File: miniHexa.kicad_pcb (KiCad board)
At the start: 2 copper layers, 20 parts, among them U1 STM32F103CBTx, U2 HT7333, Y1 8Mhz

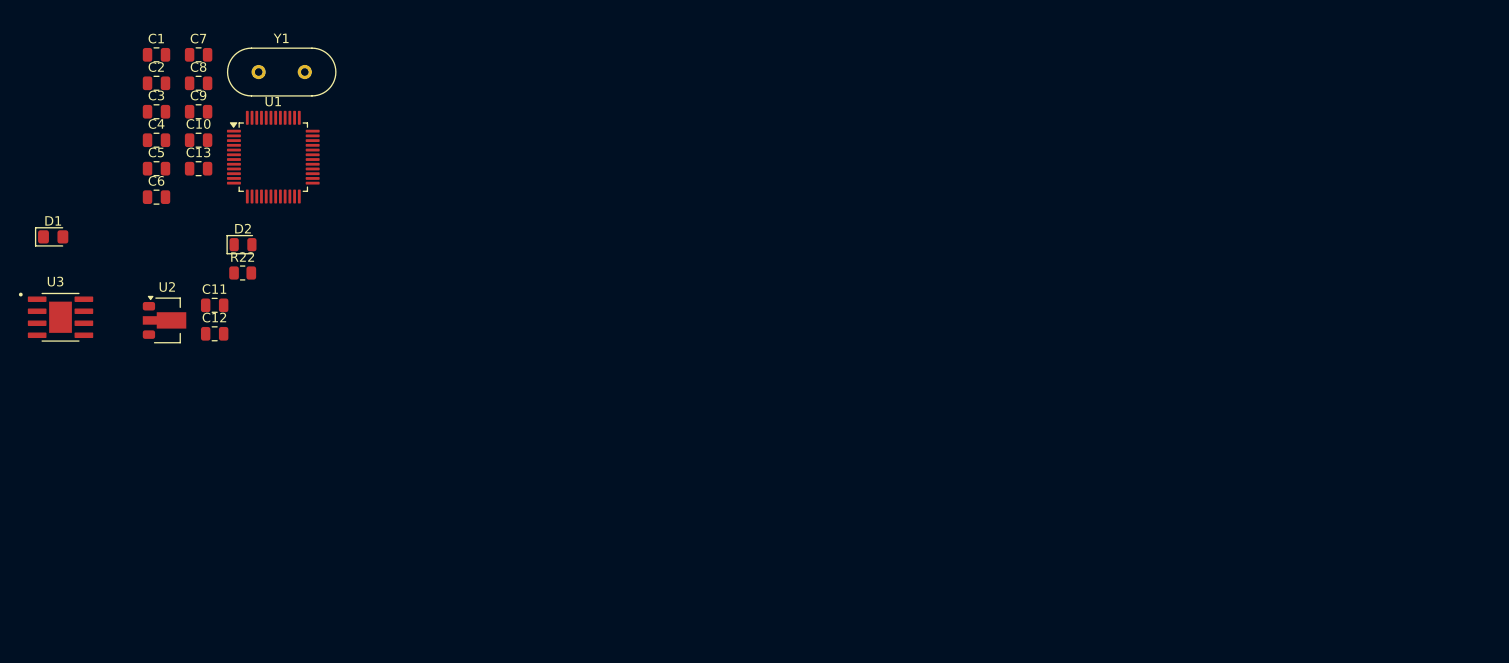
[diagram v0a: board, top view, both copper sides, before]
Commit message: Updated schema
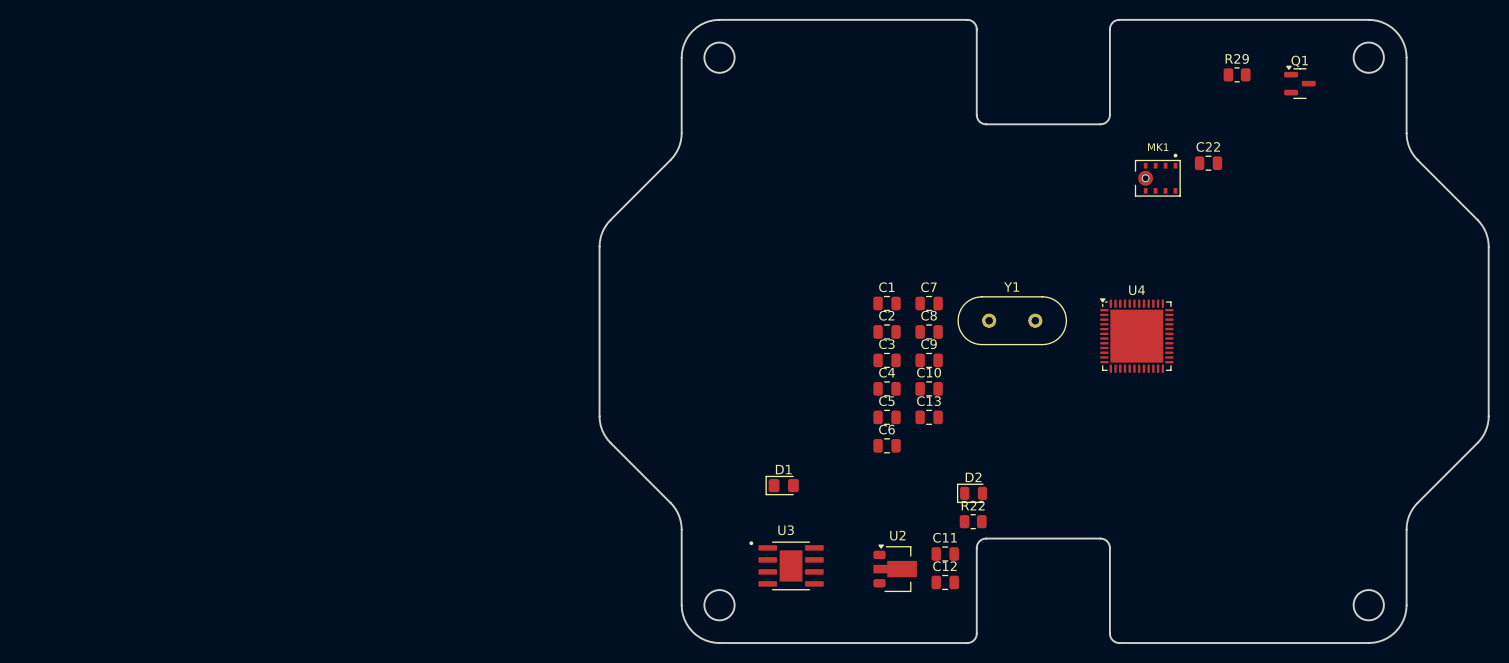
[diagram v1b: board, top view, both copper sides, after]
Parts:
- removed U1: STM32F103CBTx, Package_QFP:LQFP-48_7x7mm_P0.5mm
- added C22: 0.1uF, Capacitor_SMD:C_0805_2012Metric, F.Cu at (181.1, 67.0)
- added MK1: INMP441ACEZ-R7, Microphone:MIC_INMP441ACEZ-R7, F.Cu at (175.8, 68.6)
- added Q1: SS8050, Package_TO_SOT_SMD:SOT-23, F.Cu at (190.8, 58.5)
- added R29: 100, Resistor_SMD:R_0805_2012Metric, F.Cu at (184.2, 57.6)
- added U4: STM32F411CEUx, Package_DFN_QFN:QFN-48-1EP_7x7mm_P0.5mm_EP5.6x5.6mm, F.Cu at (173.6, 85.2)
- moved C11 81.6 mm to (153.3, 108.3)
- moved C12 81.6 mm to (153.3, 111.3)
- moved C2 81.6 mm to (147.1, 84.8)
- moved C8 81.6 mm to (151.6, 84.8)
- moved D2 81.6 mm to (156.3, 101.9)
- moved U2 81.6 mm to (148.3, 109.9)
- moved C1 81.6 mm to (147.1, 81.8)
- moved C10 81.6 mm to (151.6, 90.8)
- moved C13 81.6 mm to (151.6, 93.8)
- moved C3 81.6 mm to (147.1, 87.8)
- moved C4 81.6 mm to (147.1, 90.8)
- moved C5 81.6 mm to (147.1, 93.8)
- moved C6 81.6 mm to (147.1, 96.8)
- moved C7 81.6 mm to (151.6, 81.8)
- moved C9 81.6 mm to (151.6, 87.8)
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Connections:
- net DC_IN renamed Net-(D1-A)
- U3 pad 1: VOUT -> Net-(U3-BOOT)
- U3 pad 4: unconnected-(U3-FB-Pad4) -> FB
- U3 pad 5: unconnected-(U3-EN-Pad5) -> Net-(U3-EN)
- U3 pad 6: unconnected-(U3-GND-Pad6) -> GND
- U3 pad 7: unconnected-(U3-VIN-Pad7) -> VIN
- U3 pad 8: unconnected-(U3-SW-Pad8) -> Net-(D3-K)
- U3 pad 9: (no net) -> GND
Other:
- board outline added: 94 x 65.9 mm

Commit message: update -- i don't remeber what
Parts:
- moved Y1 10.7 mm to (161.6, 73.5)
- turned U4 to -90 degrees

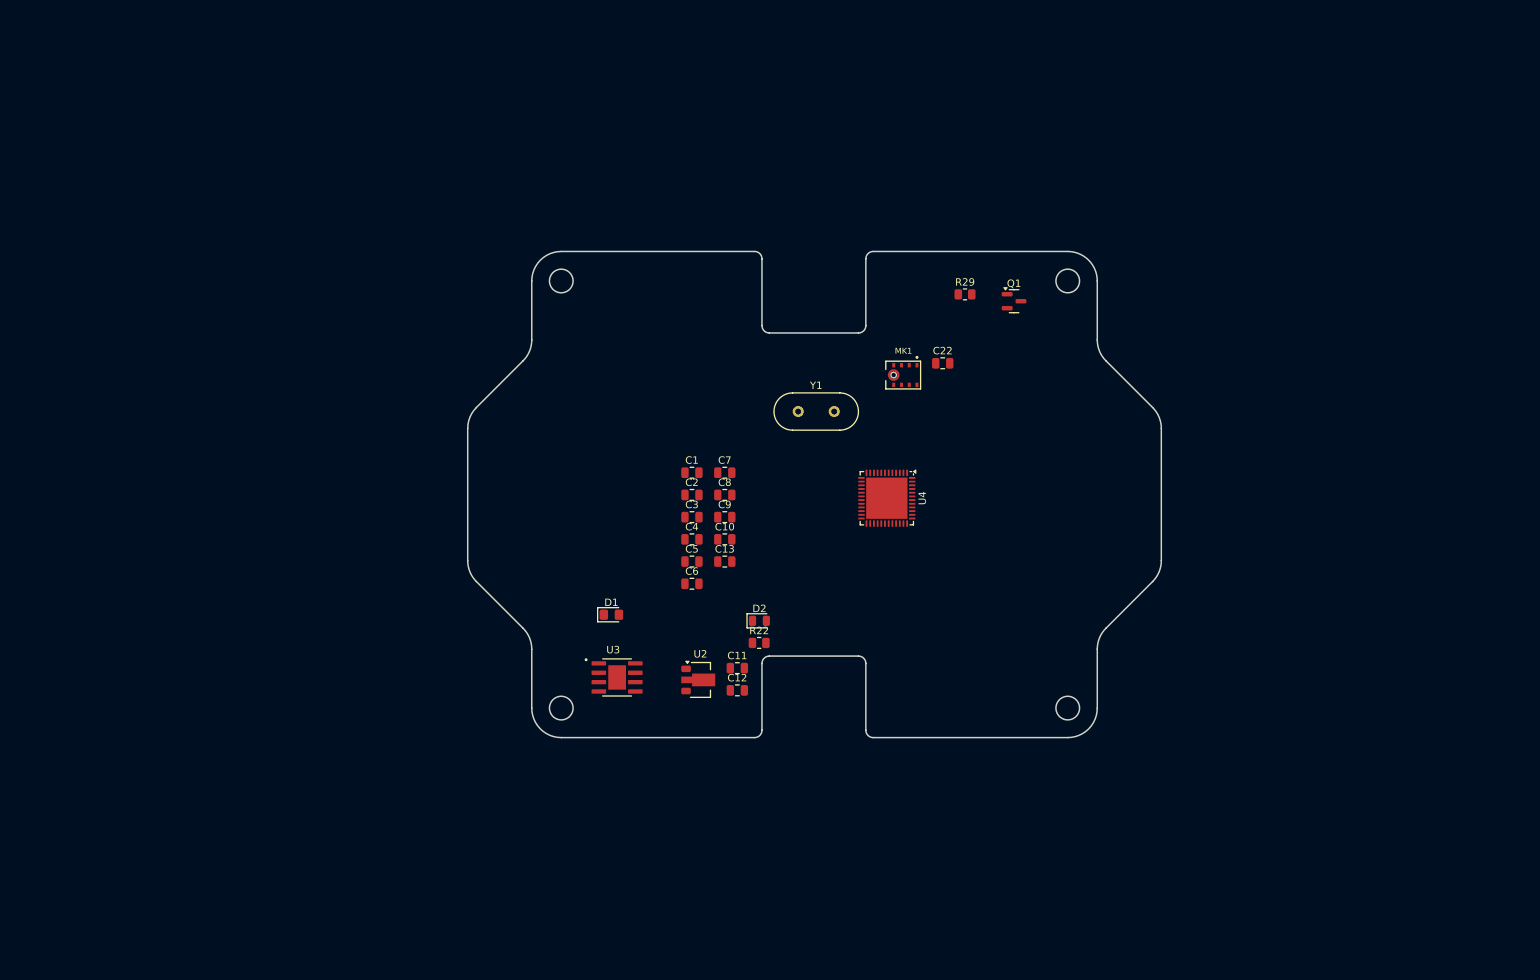
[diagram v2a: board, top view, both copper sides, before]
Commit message: assigned footprints and I2c for stm32
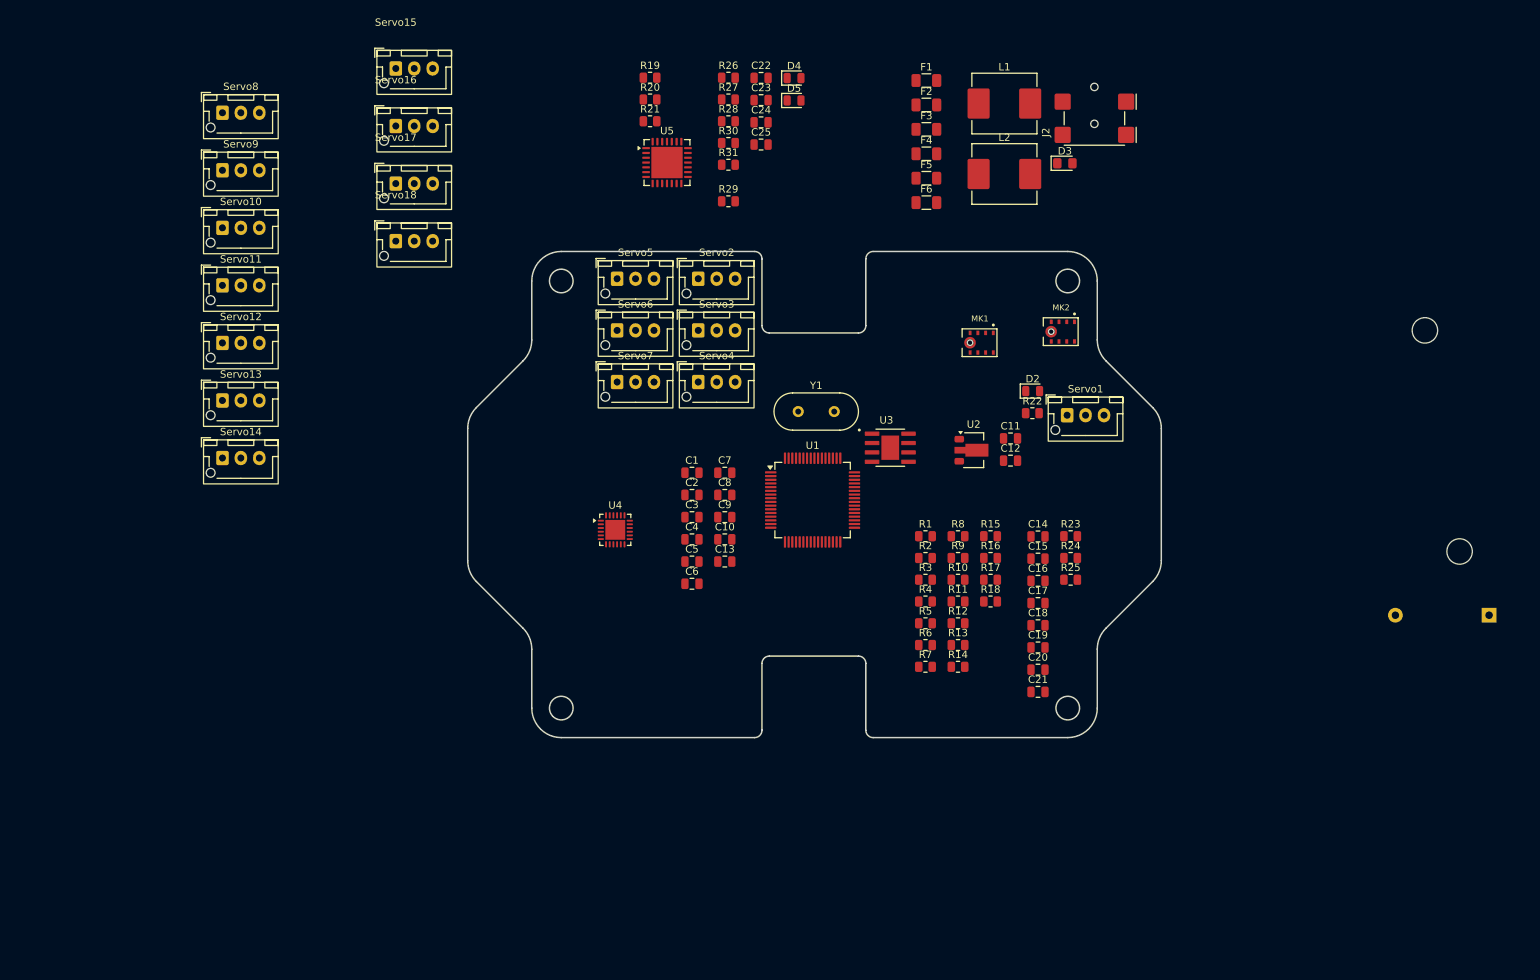
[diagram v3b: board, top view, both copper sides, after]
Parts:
- removed D1: D, Diode_SMD:D_0805_2012Metric_Pad1.15x1.40mm_HandSolder
- removed Q1: SS8050, Package_TO_SOT_SMD:SOT-23
- added BT1: Battery, Battery:BatteryHolder_Keystone_2468_2xAAA, B.Cu at (255.2, 101.1)
- added C14: 10nF, Capacitor_SMD:C_0805_2012Metric, F.Cu at (194.1, 90.4)
- added C15: 4.7uF, Capacitor_SMD:C_0805_2012Metric, F.Cu at (194.1, 93.4)
- added C16: 22uF, Capacitor_SMD:C_0805_2012Metric, F.Cu at (194.1, 96.5)
- added C17: 22uF, Capacitor_SMD:C_0805_2012Metric, F.Cu at (194.1, 99.5)
- added C18: 100uF, Capacitor_SMD:C_0805_2012Metric, F.Cu at (194.1, 102.5)
- added C19: 100uF/10v, Capacitor_SMD:C_0805_2012Metric, F.Cu at (194.1, 105.5)
- added C20: 22uF, Capacitor_SMD:C_0805_2012Metric, F.Cu at (194.1, 108.5)
- added C21: 4.7uF, Capacitor_SMD:C_0805_2012Metric, F.Cu at (194.1, 111.5)
- added C23: C, Capacitor_SMD:C_0805_2012Metric, F.Cu at (156.5, 31.3)
- added C24: C, Capacitor_SMD:C_0805_2012Metric, F.Cu at (156.5, 34.3)
- added C25: C, Capacitor_SMD:C_0805_2012Metric, F.Cu at (156.5, 37.3)
- added D3: P6SMB550A, Diode_SMD:D_0805_2012Metric_Pad1.15x1.40mm_HandSolder, F.Cu at (197.7, 39.8)
- added D4: LED, LED_SMD:LED_0805_2012Metric, F.Cu at (161.0, 28.3)
- added D5: LED, LED_SMD:LED_0805_2012Metric, F.Cu at (161.0, 31.3)
- added F1: 1A, Fuse:Fuse_1206_3216Metric, F.Cu at (178.9, 28.6)
- added F2: 1A, Fuse:Fuse_1206_3216Metric, F.Cu at (178.9, 31.9)
- added F3: 1A, Fuse:Fuse_1206_3216Metric, F.Cu at (178.9, 35.2)
- added F4: 1A, Fuse:Fuse_1206_3216Metric, F.Cu at (178.9, 38.6)
- added F5: 1A, Fuse:Fuse_1206_3216Metric, F.Cu at (178.9, 41.9)
- added F6: 1A, Fuse:Fuse_1206_3216Metric, F.Cu at (178.9, 45.2)
- added J2: 12v DC, Connector_BarrelJack:BarrelJack_Wuerth_694102107102_1.0x3.9mm, F.Cu at (201.7, 32.6)
- added L1: 15uH, Inductor_SMD:L_APV_APH0850, F.Cu at (189.5, 31.8)
- added L2: 15uH, Inductor_SMD:L_APV_APH0850, F.Cu at (189.5, 41.3)
- added MK2: INMP441-R, Audio_Module:MIC_INMP441ACEZ-R7, F.Cu at (197.1, 62.7)
- added R1: 1k, Resistor_SMD:R_0805_2012Metric, F.Cu at (178.8, 90.4)
- added R10: 1k, Resistor_SMD:R_0805_2012Metric, F.Cu at (183.2, 96.3)
- added R11: 1k, Resistor_SMD:R_0805_2012Metric, F.Cu at (183.2, 99.2)
- added R12: 1k, Resistor_SMD:R_0805_2012Metric, F.Cu at (183.2, 102.2)
- added R13: 1k, Resistor_SMD:R_0805_2012Metric, F.Cu at (183.2, 105.2)
- added R14: 1k, Resistor_SMD:R_0805_2012Metric, F.Cu at (183.2, 108.1)
- added R15: 1k, Resistor_SMD:R_0805_2012Metric, F.Cu at (187.6, 90.4)
- added R16: 1k, Resistor_SMD:R_0805_2012Metric, F.Cu at (187.6, 93.3)
- added R17: 1k, Resistor_SMD:R_0805_2012Metric, F.Cu at (187.6, 96.3)
- added R18: 1k, Resistor_SMD:R_0805_2012Metric, F.Cu at (187.6, 99.2)
- added R19: R, Resistor_SMD:R_0805_2012Metric, F.Cu at (141.5, 28.2)
- added R2: 1k, Resistor_SMD:R_0805_2012Metric, F.Cu at (178.8, 93.3)
- added R20: R, Resistor_SMD:R_0805_2012Metric, F.Cu at (141.5, 31.2)
- added R21: R, Resistor_SMD:R_0805_2012Metric, F.Cu at (141.5, 34.1)
- added R23: 100K, Resistor_SMD:R_0805_2012Metric, F.Cu at (198.5, 90.4)
- added R24: 10k_0.1%, Resistor_SMD:R_0805_2012Metric, F.Cu at (198.5, 93.3)
- added R25: 3.16k, Resistor_SMD:R_0805_2012Metric, F.Cu at (198.5, 96.3)
- added R26: R, Resistor_SMD:R_0805_2012Metric, F.Cu at (152.1, 28.2)
- added R27: R, Resistor_SMD:R_0805_2012Metric, F.Cu at (152.1, 31.2)
- added R28: R, Resistor_SMD:R_0805_2012Metric, F.Cu at (152.1, 34.1)
- added R3: 1k, Resistor_SMD:R_0805_2012Metric, F.Cu at (178.8, 96.3)
- added R30: R, Resistor_SMD:R_0805_2012Metric, F.Cu at (152.1, 37.1)
- added R31: R, Resistor_SMD:R_0805_2012Metric, F.Cu at (152.1, 40.0)
- added R4: 1k, Resistor_SMD:R_0805_2012Metric, F.Cu at (178.8, 99.2)
- added R5: 1k, Resistor_SMD:R_0805_2012Metric, F.Cu at (178.8, 102.2)
- added R6: 1k, Resistor_SMD:R_0805_2012Metric, F.Cu at (178.8, 105.2)
- added R7: 1k, Resistor_SMD:R_0805_2012Metric, F.Cu at (178.8, 108.1)
- added R8: 1k, Resistor_SMD:R_0805_2012Metric, F.Cu at (183.2, 90.4)
- added R9: 1k, Resistor_SMD:R_0805_2012Metric, F.Cu at (183.2, 93.3)
- added Servo1: Conn_01x03_Pin, Connector_JST:JST_XH_B3B-XH-AM_1x03_P2.50mm_Vertical, F.Cu at (198.0, 74.0)
- added Servo10: Conn_01x03_Pin, Connector_JST:JST_XH_B3B-XH-AM_1x03_P2.50mm_Vertical, F.Cu at (83.5, 48.6)
- added Servo11: Conn_01x03_Pin, Connector_JST:JST_XH_B3B-XH-AM_1x03_P2.50mm_Vertical, F.Cu at (83.5, 56.4)
- added Servo12: Conn_01x03_Pin, Connector_JST:JST_XH_B3B-XH-AM_1x03_P2.50mm_Vertical, F.Cu at (83.5, 64.2)
- added Servo13: Conn_01x03_Pin, Connector_JST:JST_XH_B3B-XH-AM_1x03_P2.50mm_Vertical, F.Cu at (83.5, 72.0)
- added Servo14: Conn_01x03_Pin, Connector_JST:JST_XH_B3B-XH-AM_1x03_P2.50mm_Vertical, F.Cu at (83.5, 79.8)
- added Servo15: Conn_01x03_Pin, Connector_JST:JST_XH_B3B-XH-AM_1x03_P2.50mm_Vertical, F.Cu at (107.0, 27.0)
- added Servo16: Conn_01x03_Pin, Connector_JST:JST_XH_B3B-XH-AM_1x03_P2.50mm_Vertical, F.Cu at (107.0, 34.8)
- added Servo17: Conn_01x03_Pin, Connector_JST:JST_XH_B3B-XH-AM_1x03_P2.50mm_Vertical, F.Cu at (107.0, 42.6)
- added Servo18: Conn_01x03_Pin, Connector_JST:JST_XH_B3B-XH-AM_1x03_P2.50mm_Vertical, F.Cu at (107.0, 50.4)
- added Servo2: Conn_01x03_Pin, Connector_JST:JST_XH_B3B-XH-AM_1x03_P2.50mm_Vertical, F.Cu at (148.0, 55.5)
- added Servo3: Conn_01x03_Pin, Connector_JST:JST_XH_B3B-XH-AM_1x03_P2.50mm_Vertical, F.Cu at (148.0, 62.5)
- added Servo4: Conn_01x03_Pin, Connector_JST:JST_XH_B3B-XH-AM_1x03_P2.50mm_Vertical, F.Cu at (148.0, 69.5)
- added Servo5: Conn_01x03_Pin, Connector_JST:JST_XH_B3B-XH-AM_1x03_P2.50mm_Vertical, F.Cu at (137.0, 55.5)
- added Servo6: Conn_01x03_Pin, Connector_JST:JST_XH_B3B-XH-AM_1x03_P2.50mm_Vertical, F.Cu at (137.0, 62.5)
- added Servo7: Conn_01x03_Pin, Connector_JST:JST_XH_B3B-XH-AM_1x03_P2.50mm_Vertical, F.Cu at (137.0, 69.5)
- added Servo8: Conn_01x03_Pin, Connector_JST:JST_XH_B3B-XH-AM_1x03_P2.50mm_Vertical, F.Cu at (83.5, 33.0)
- added Servo9: Conn_01x03_Pin, Connector_JST:JST_XH_B3B-XH-AM_1x03_P2.50mm_Vertical, F.Cu at (83.5, 40.8)
- added U1: STM32F401RETx, Package_QFP:LQFP-64_10x10mm_P0.5mm, F.Cu at (163.5, 85.5)
- added U5: PCA9685BS, Package_DFN_QFN:QFN-28-1EP_6x6mm_P0.65mm_EP4.25x4.25mm, F.Cu at (143.8, 39.8)
- C22: value 0.1uF -> C
- MK1: value INMP441ACEZ-R7 -> INMP441-L; footprint Microphone:MIC_INMP441ACEZ-R7 -> Audio_Module:MIC_INMP441ACEZ-R7
- R29: value 100 -> 100k
- U3: value ~ -> RT8289GSP
- U4: value STM32F411CEUx -> BQ25886RGE; footprint Package_DFN_QFN:QFN-48-1EP_7x7mm_P0.5mm_EP5.6x5.6mm -> Package_DFN_QFN:Texas_RGE0024H_VQFN-24-1EP_4x4mm_P0.5mm_EP2.7x2.7mm
- Y1: value 8Mhz -> 16Mhz
- moved C11 48.4 mm to (190.3, 77.1)
- moved C12 48.4 mm to (190.3, 80.2)
- moved D2 48.4 mm to (193.3, 70.7)
- moved R22 48.4 mm to (193.3, 73.7)
- moved U2 48.4 mm to (185.3, 78.7)
- moved U3 48.4 mm to (174.0, 78.4)
- moved C22 45.9 mm to (156.5, 28.3)
- moved U4 37.1 mm to (136.8, 89.5), turned to 0 degrees
- moved R29 34.5 mm to (152.1, 45.0)
- moved MK1 11.2 mm to (186.1, 64.2)
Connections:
- C1 pad 2: Net-(U4-PH0) -> Net-(U1-PH0)
- C13 pad 1: Net-(U4-NRST) -> Net-(U1-NRST)
- C2 pad 1: Net-(U4-PH1) -> Net-(U1-PH1)
- C22 pad 1: +3.3V -> Net-(BT1-+)
- C22 pad 2: Net-(C22-Pad2) -> GND
- MK1 pad 1: Net-(MK1-SCK) -> MIC_SCK
- MK1 pad 2: Net-(MK1-SD) -> MIC_WS
- MK1 pad 3: Net-(MK1-WS) -> MIC_SD
- MK1 pad 4: unconnected-(MK1-L/R-Pad4) -> GND
- MK1 pad 5: Net-(C22-Pad2) -> GND
- MK1 pad 6: Net-(C22-Pad2) -> GND
- MK1 pad 8: CHIPEN_MIC -> CHIPEN_MIC_L
- MK1 pad 9: Net-(C22-Pad2) -> GND
- R29 pad 1: Net-(MK1-SD) -> MIC_WS
- U2 pad 2: +5V -> +3.3V
- U2 pad 3: +3.3V -> +5V
- U4 pad 1: +3.3V -> unconnected-(U4-D--Pad1)
- U4 pad 10: unconnected-(U4-PA0-Pad10) -> Net-(U4-ICHGSET)
- U4 pad 11: SERVO1 -> Net-(U4-REGN)
- U4 pad 12: SERVO2 -> Net-(U4-BTST)
- U4 pad 13: SERVO3 -> Net-(BT1-+)
- U4 pad 14: Net-(MK1-WS) -> Net-(BT1-+)
- U4 pad 15: Net-(MK1-SCK) -> VIN
- U4 pad 16: SERVO6 -> VIN
- U4 pad 17: Net-(MK1-SD) -> Net-(C24-Pad1)
- U4 pad 18: SERVO8 -> Net-(C24-Pad1)
- U4 pad 19: SERVO9 -> GND
- U4 pad 2: unconnected-(U4-PC13-Pad2) -> Net-(D4-K)
- U4 pad 20: SERVO10 -> GND
- U4 pad 21: SERVO11 -> Net-(C23-Pad2)
- U4 pad 22: unconnected-(U4-VCAP1-Pad22) -> Net-(C23-Pad2)
- U4 pad 23: Net-(U4-VSS-Pad23) -> Net-(U4-VBUS)
- U4 pad 24: +3.3V -> unconnected-(U4-D+-Pad24)
- U4 pad 25: SERVO12 -> GND
- U4 pad 4: unconnected-(U4-PC15-Pad4) -> GND
- U4 pad 5: Net-(U4-PH0) -> unconnected-(U4-OTG-Pad5)
- U4 pad 6: Net-(U4-PH1) -> Net-(U4-VSET)
- U4 pad 7: Net-(U4-NRST) -> unconnected-(U4-TS-Pad7)
- U4 pad 8: unconnected-(U4-VSSA-Pad8) -> Net-(U4-ILIM)
- U4 pad 9: +3.3V -> Net-(D5-K)
- Y1 pad 1: Net-(U4-PH1) -> Net-(U1-PH1)
- Y1 pad 2: Net-(U4-PH0) -> Net-(U1-PH0)
